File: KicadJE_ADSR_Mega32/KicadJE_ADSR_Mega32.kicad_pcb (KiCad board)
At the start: 2 copper layers, 100 x 100 mm, 100 parts, among them J101 In, J102 Out, J201 AVR-ISP-6, J202 UART, J301 In, J302 +5V reg/doepfer, J303 Out, J304 In, J305 CV doepfer, P101 Doepfer_Power_16pin, P302 Doepfer_Power_16pin, Q301 BC337, Q302 PZT2222A, U201 ATmega32A-AU, U301 L78L05_TO92, U302 PT2399, Y201 16MHz

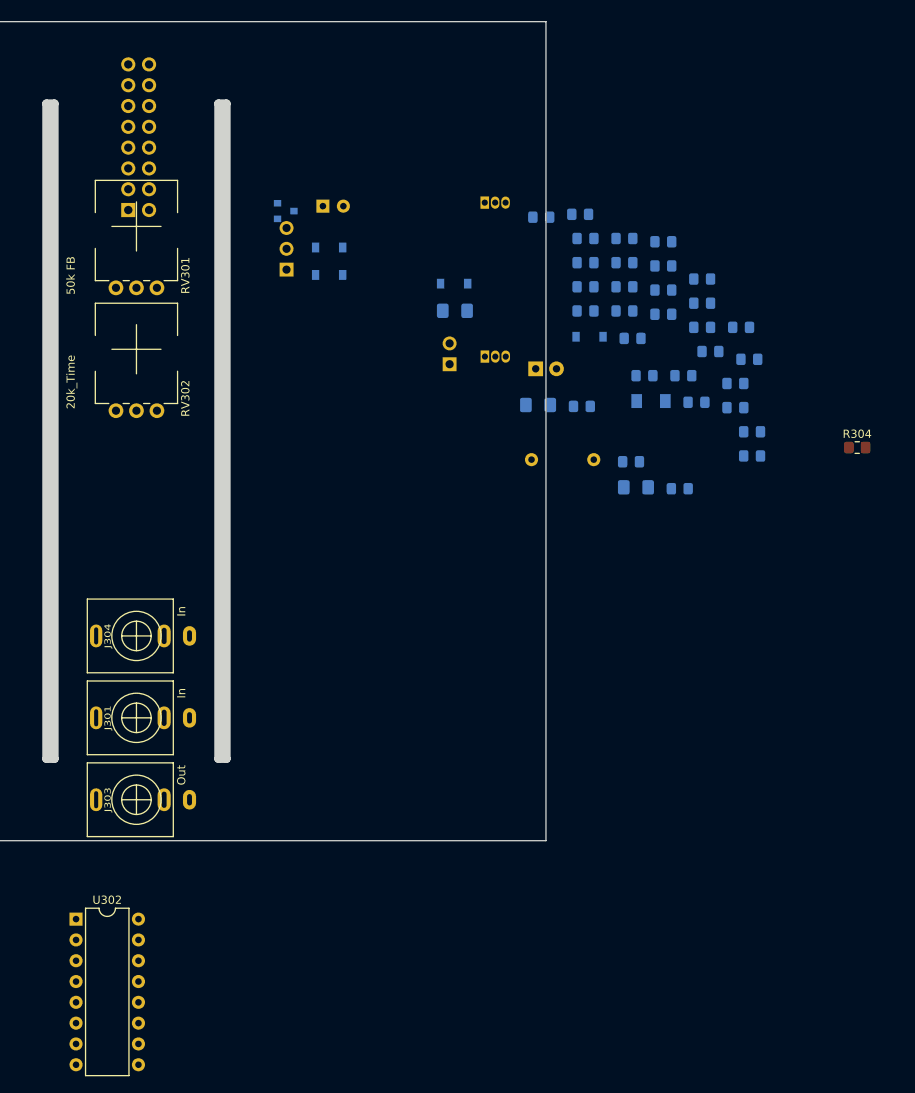
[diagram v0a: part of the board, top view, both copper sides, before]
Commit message: pwr components place - PT2399
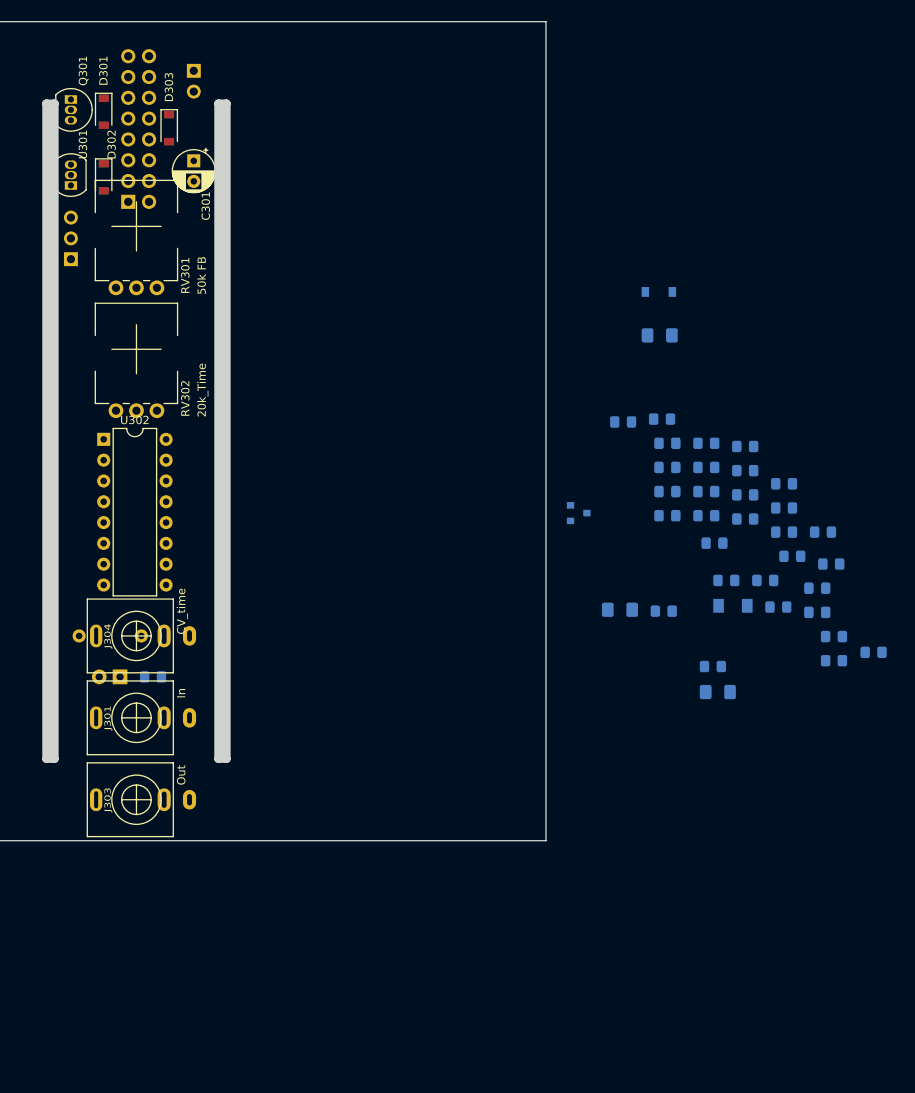
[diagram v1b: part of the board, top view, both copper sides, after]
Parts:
- C301, D301, D302, D303, Q301, U301: moved to F.Cu
- J304: value In -> CV_time
- R304: moved to B.Cu
- moved R317 68.3 mm to (102.0, 130.0)
- moved D301 65.4 mm to (96.0, 61.0), turned to 270 degrees
- moved D306 63.2 mm to (98.0, 130.0), turned to 180 degrees
- moved R316 59.3 mm to (93.0, 125.0)
- moved U302 58.7 mm to (96.0, 101.0)
- moved U301 54.7 mm to (92.0, 70.0), turned to 90 degrees
- moved Q301 52.1 mm to (92.0, 59.5), turned to 270 degrees
- moved Q302 51.4 mm to (154.0, 110.0)
- moved J305 47.5 mm to (107.0, 56.0), turned to 180 degrees
- moved D302 28.8 mm to (96.0, 69.0), turned to 270 degrees
- moved C307 26.9 mm to (185.2, 128.0)
- moved C302 26.9 mm to (164.8, 110.3)
- moved C303 26.9 mm to (159.0, 121.8)
- moved C304 26.9 mm to (164.8, 104.4)
- moved C306 26.9 mm to (185.2, 125.1)
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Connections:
- net Net-(C304-Pad2) renamed 5Vreg
- D306 pad 2: CV_B -> CV

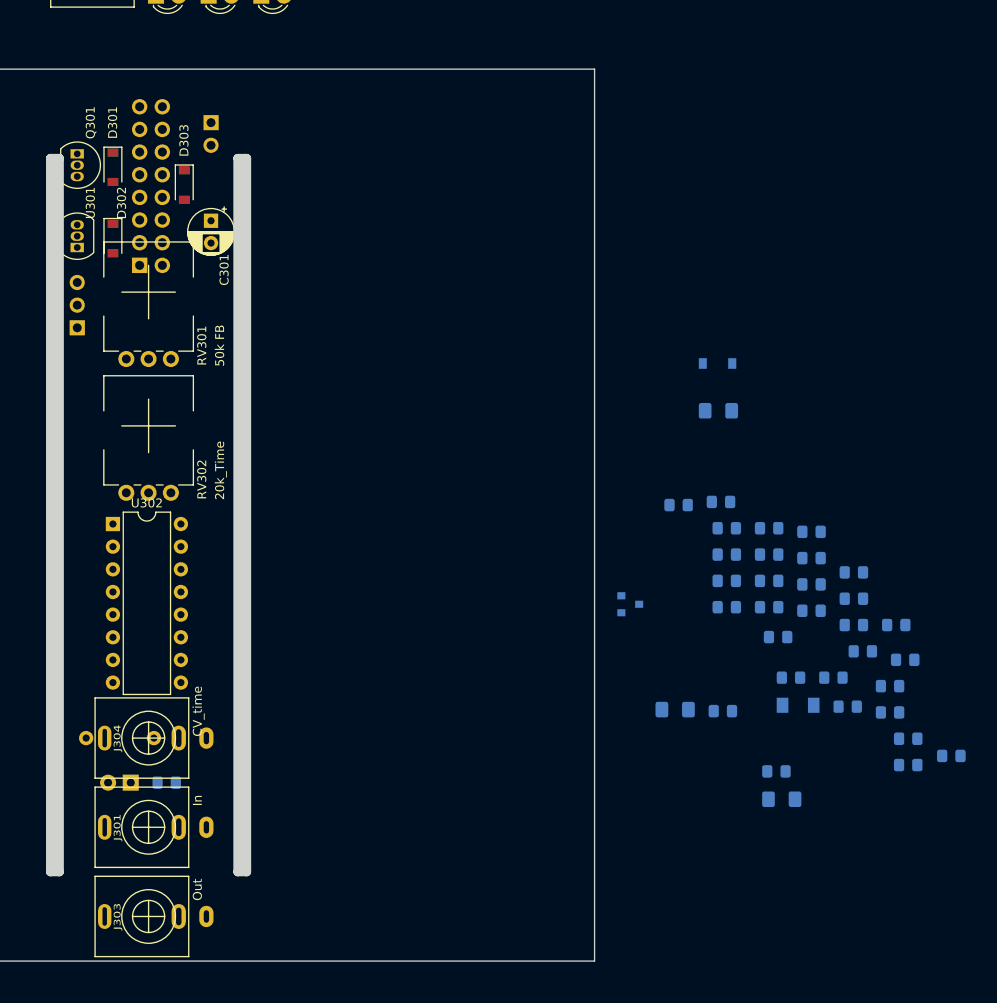
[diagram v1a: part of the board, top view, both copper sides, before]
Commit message: PT2399 - PWR and VCO placed
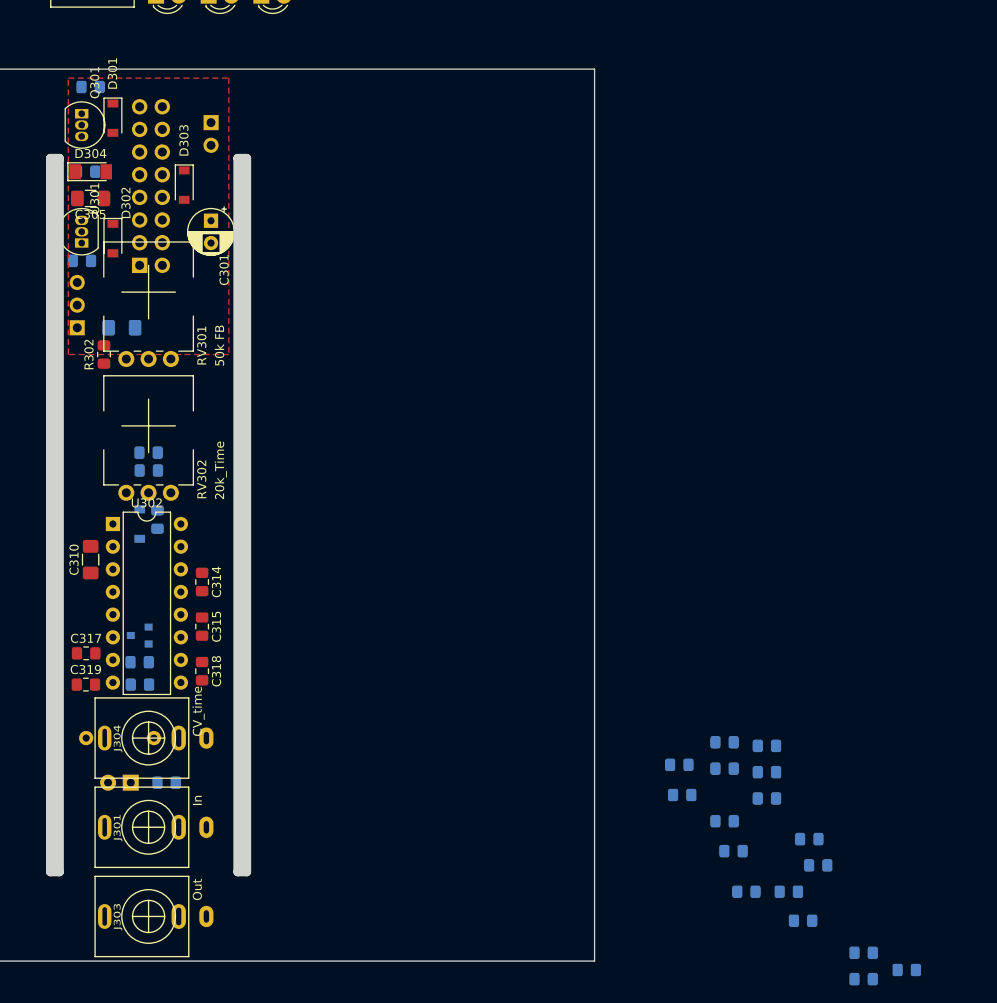
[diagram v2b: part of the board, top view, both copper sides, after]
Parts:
- C305, C310, C314, C315, C317, C318, C319, D304, R302: moved to F.Cu
- moved C305 102.7 mm to (93.5, 64.5), turned to 180 degrees
- moved R301 99.9 mm to (93.5, 52.0)
- moved D304 99.4 mm to (93.5, 61.5)
- moved R302 95.6 mm to (95.0, 82.0), turned to 90 degrees
- moved C319 91.9 mm to (93.0, 119.0)
- moved C317 90.9 mm to (93.0, 115.5)
- moved C302 86.8 mm to (93.0, 61.5), turned to 180 degrees
- moved R314 84.3 mm to (99.0, 116.5), turned to 180 degrees
- moved C320 80.3 mm to (100.0, 95.0)
- moved C304 79.4 mm to (92.5, 71.5), turned to 180 degrees
- moved C303 75.4 mm to (97.0, 79.0), turned to 180 degrees
- moved C314 73.1 mm to (106.0, 107.5), turned to 270 degrees
- moved C310 72.3 mm to (93.5, 105.0), turned to 90 degrees
- moved R315 71.5 mm to (99.0, 119.0)
- moved D305 67.2 mm to (99.0, 101.0), turned to 90 degrees
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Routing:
- added copper zone on F.Cu, net GND

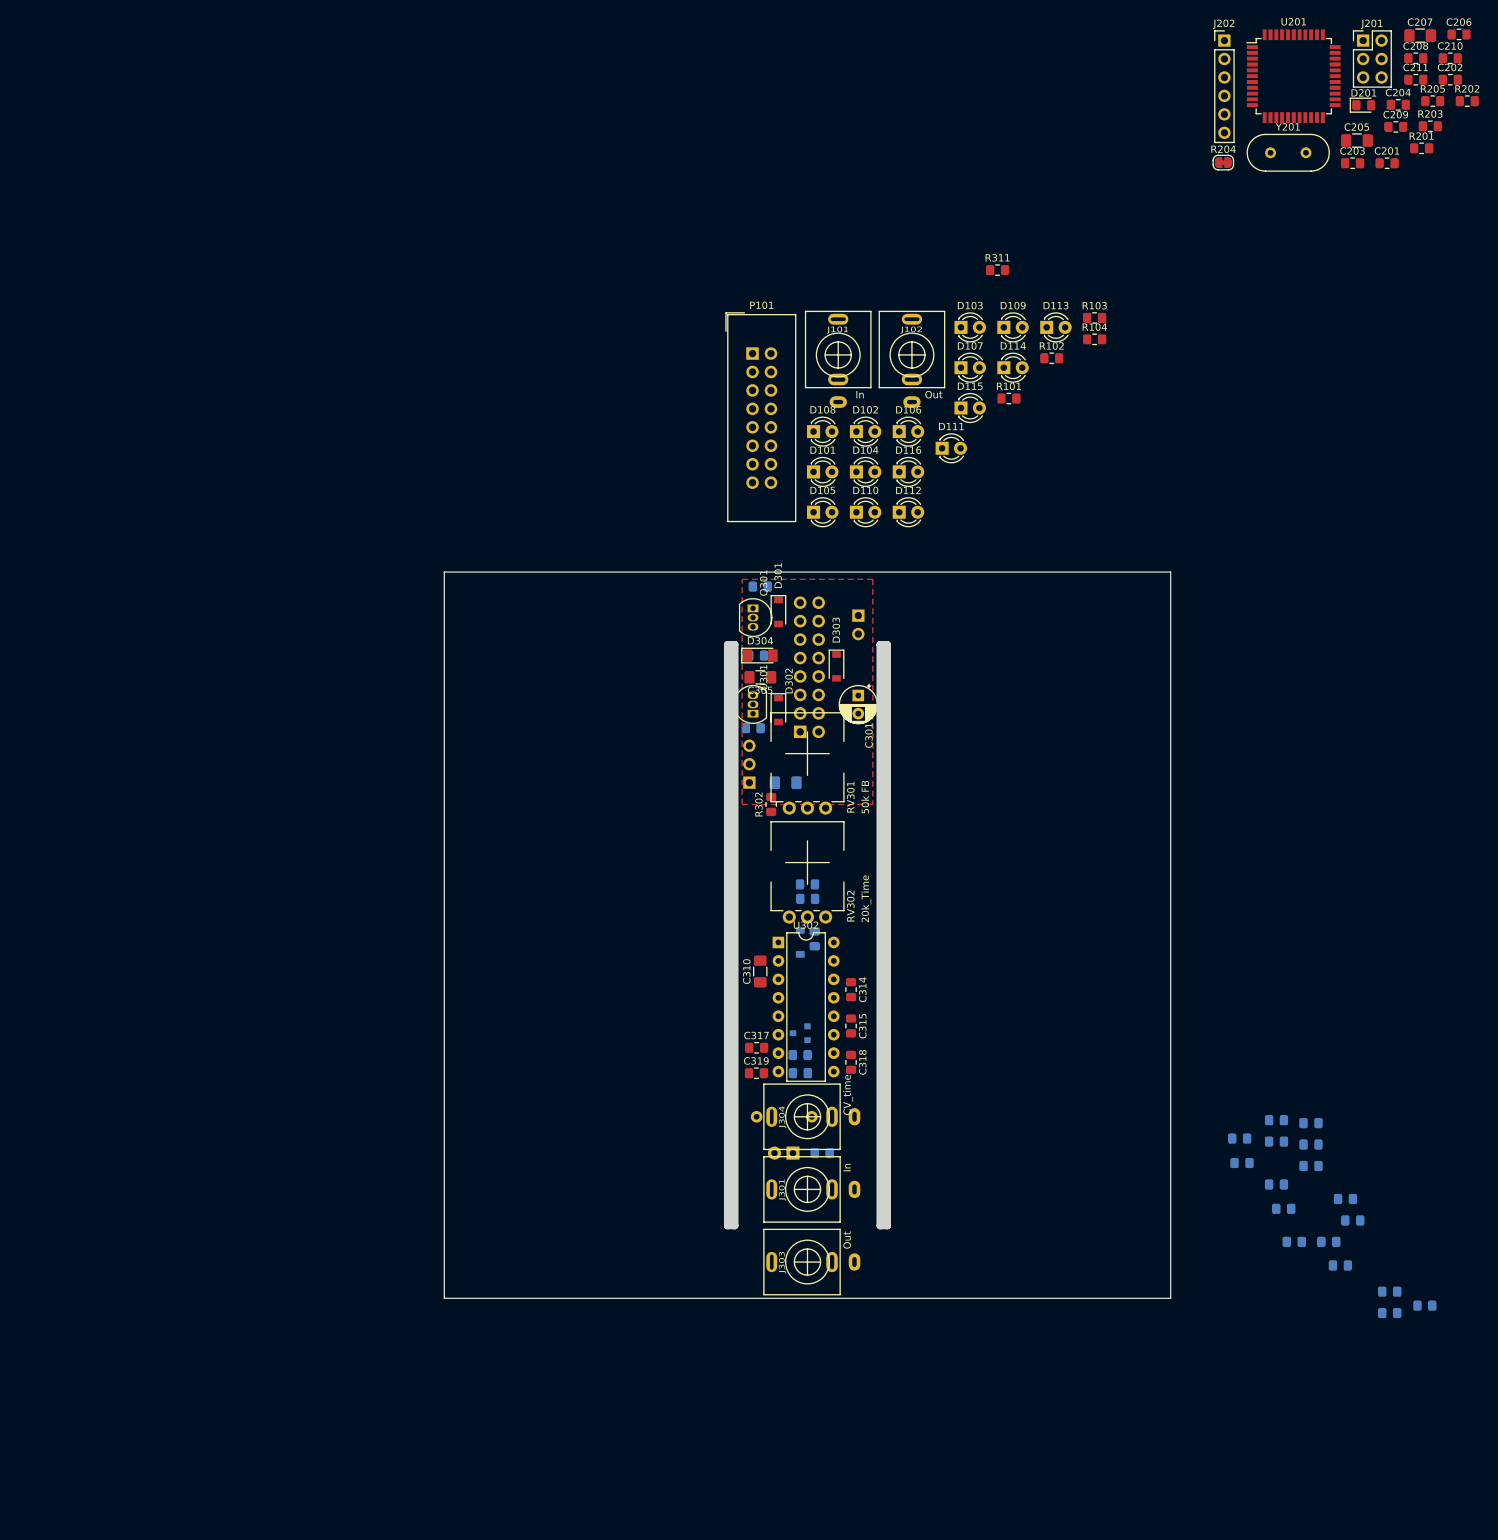
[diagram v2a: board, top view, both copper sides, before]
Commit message: PT2399 routed
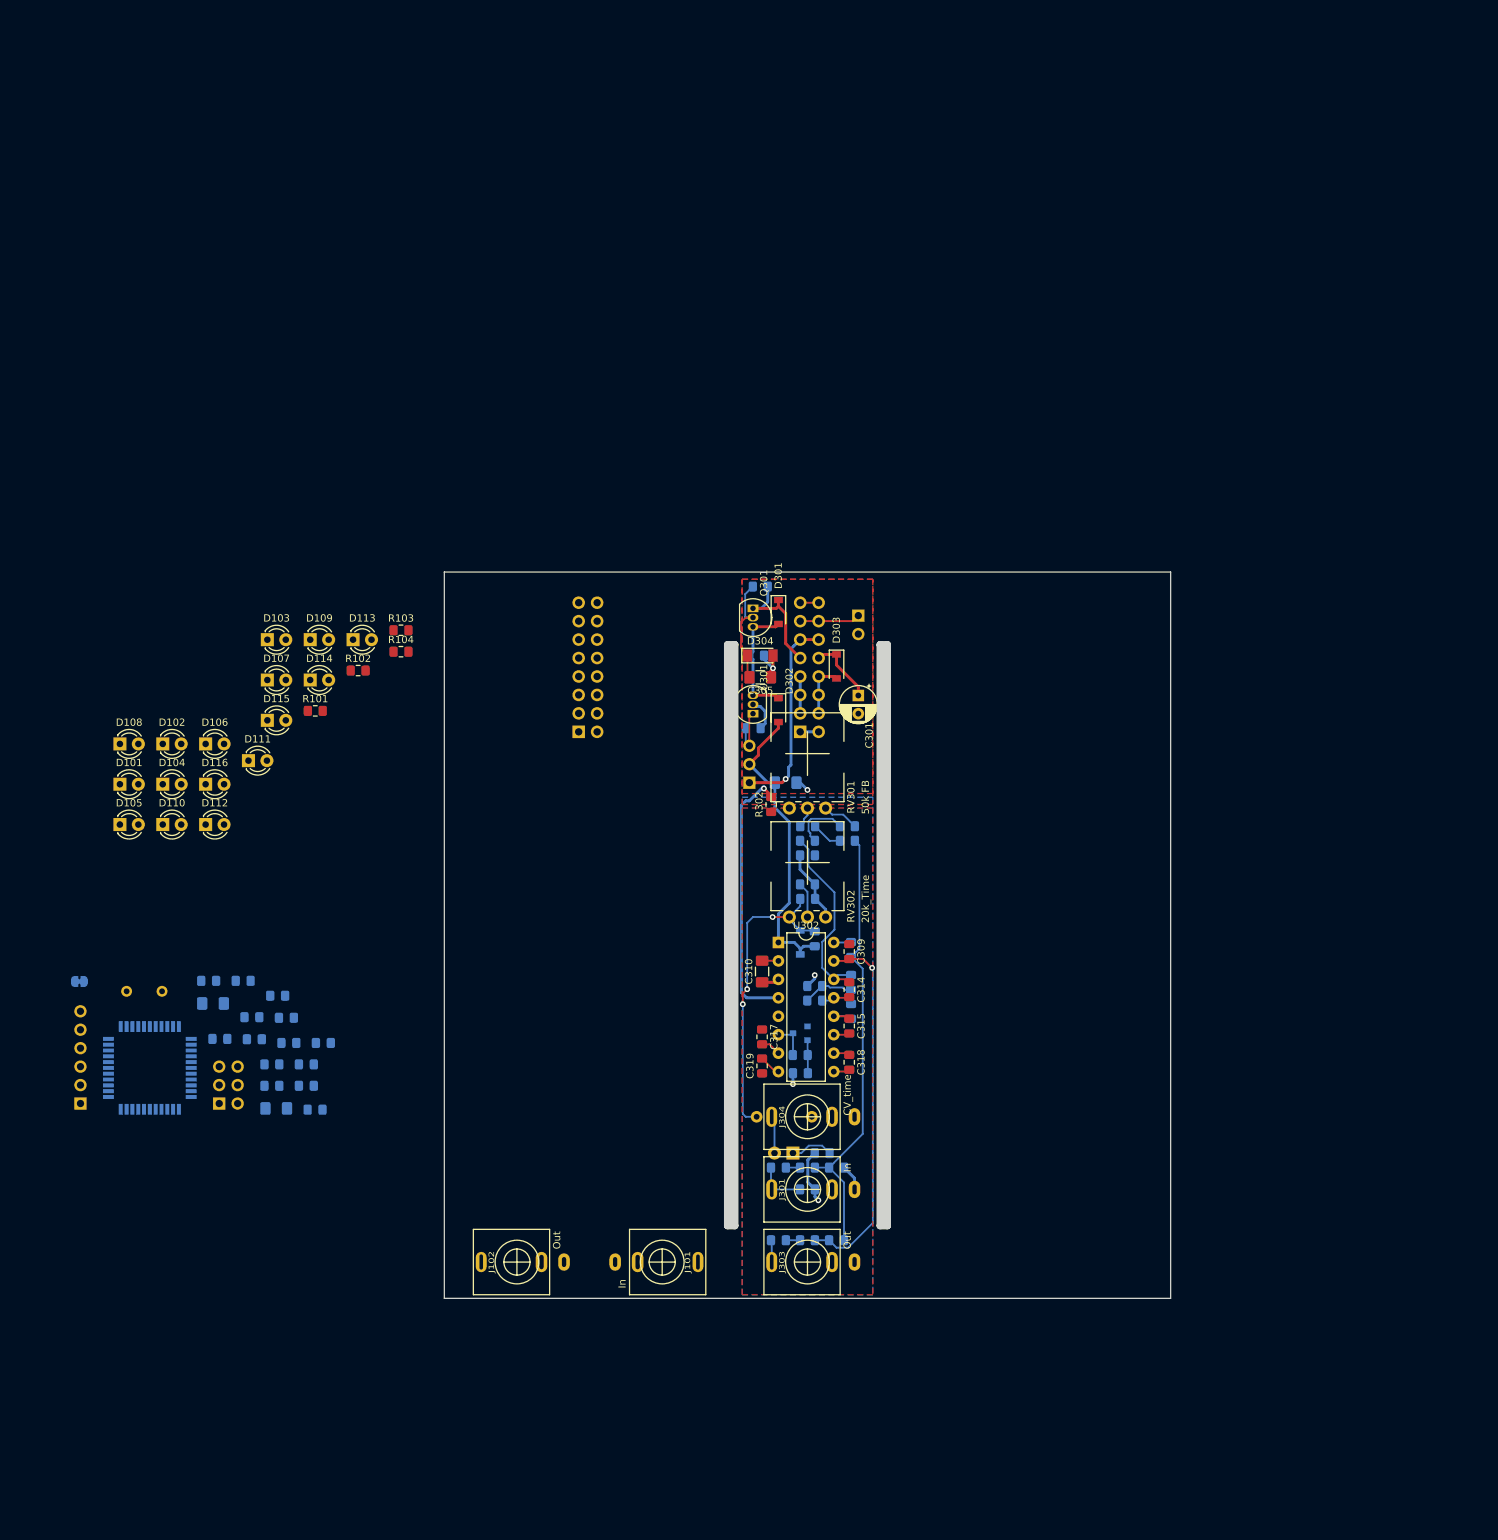
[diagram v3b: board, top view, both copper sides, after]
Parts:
- C201, C202, C203, C204, C205, C206, C207, C208, C209, C210, C211, D201, J201, J202, P101, R201, R202, R203, R204, R205, R311, U201, Y201: moved to B.Cu
- C309: moved to F.Cu
- moved C206 216.2 mm to (32.2, 124.0)
- moved C207 215.9 mm to (26.9, 123.9)
- moved J201 215.0 mm to (19.0, 123.2)
- moved J202 215.0 mm to (-0.09, 123.2)
- moved C208 211.7 mm to (26.3, 120.7)
- moved C210 211.7 mm to (31.0, 120.7)
- moved U201 208.5 mm to (9.46, 118.3)
- moved C202 207.8 mm to (31.0, 117.8)
- moved C211 207.8 mm to (26.3, 117.8)
- moved R202 204.0 mm to (33.3, 114.8)
- moved R205 204.0 mm to (28.6, 114.8)
- moved C204 203.4 mm to (23.8, 114.3)
- moved D201 203.3 mm to (19.1, 114.3)
- moved R203 199.7 mm to (28.3, 111.4)
- moved C209 199.6 mm to (23.5, 111.3)
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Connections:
- C307 pad 2: In -> In2399
- C311 pad 2: Out -> Out2399
- J101 pad T: In -> (no net)
- J102 pad T: Out -> (no net)
- J301 pad T: In -> In2399
- J303 pad T: Out -> Out2399
- R304 pad 2: In -> In2399
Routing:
- net GND: track 0.00 -> 61.6 mm, vias 0 -> 3
- net Net-(C306-Pad1): track 0.00 -> 61.1 mm
- net DelayLine_In: track 0.00 -> 50.9 mm, vias 0 -> 1
- net Net-(C320-Pad1): track 0.00 -> 42.4 mm, vias 0 -> 3
- net +5VA: track 0.00 -> 41.9 mm
- net +5V: track 0.00 -> 27.8 mm, vias 0 -> 1
- net LFP2-Out: track 0.00 -> 27.3 mm
- net +12Vb: track 0.00 -> 26.9 mm
- net GNDA: track 0.00 -> 26.9 mm, vias 0 -> 3
- net /KicadJE-EU1-PT2399_sub/7v5: track 0.00 -> 17.2 mm
- net Net-(C305-Pad2): track 0.00 -> 15.7 mm
- net Net-(C316-Pad1): track 0.00 -> 9.02 mm
- net CV_B: track 0.00 -> 8.31 mm
- net Net-(C312-Pad1): track 0.00 -> 7.94 mm
- net 5Vreg: track 0.00 -> 7.25 mm
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- added copper zone on F.Cu, net +5V
- added copper zone on B.Cu, net +5VA
- added copper zone on F.Cu, net GNDA
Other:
- net class Power added: clearance 0.2, trace_width 0.4, via_dia 0.8, via_drill 0.4
